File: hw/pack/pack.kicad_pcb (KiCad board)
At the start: 4 copper layers, 73.4 x 35 mm, 75 parts, among them J1 3.5mm locking, J2 USB-C, J3 SWD, Q1 DMG2305UX, SW1 recessed slide, U1 BT40NE, U2 PCM1840, U3 OPA1656, U4 TPS61023, U5 TLV75533P, U6 TLV75533P, U7 USBLC6-2SC6

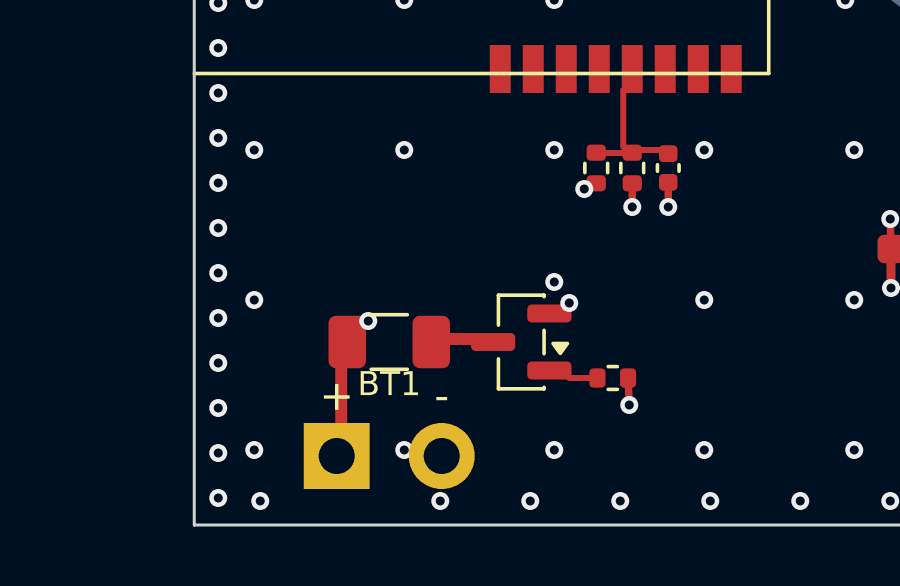
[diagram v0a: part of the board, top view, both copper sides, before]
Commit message: hw/pack: enclosure fit (fit.py + CadQuery test), mech outline from the layout, layout tests (#34)
mech/pack.py takes the real outline (73.4 x 35 mm, post notch), z0 +1.4 mm so
the module antenna clears the clip bosses, and the antenna overhang as a part.
fit.py checks board/parts/openings/lid features without CadQuery and renders
fit_top/fit_side.png; tests/mech/test_pack_fit.py does it with the STEP.
tests/test_pack_layout.py: DRC 0 errors, fab outputs fresh, netlist parity.

Co-Authored-By: Claude Opus 5.5 <noreply@anthropic.com>
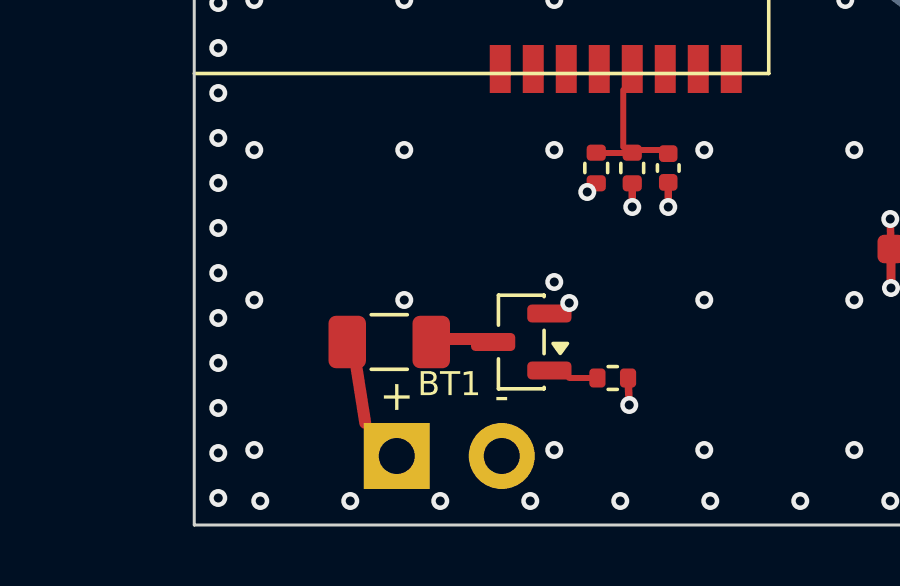
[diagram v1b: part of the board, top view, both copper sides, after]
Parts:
- moved BT1 2.00 mm to (80.5, 104.2)
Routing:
- net BAT+: track 10.5 -> 11.4 mm, vias 2 -> 1
- net GND: vias 205 -> 206

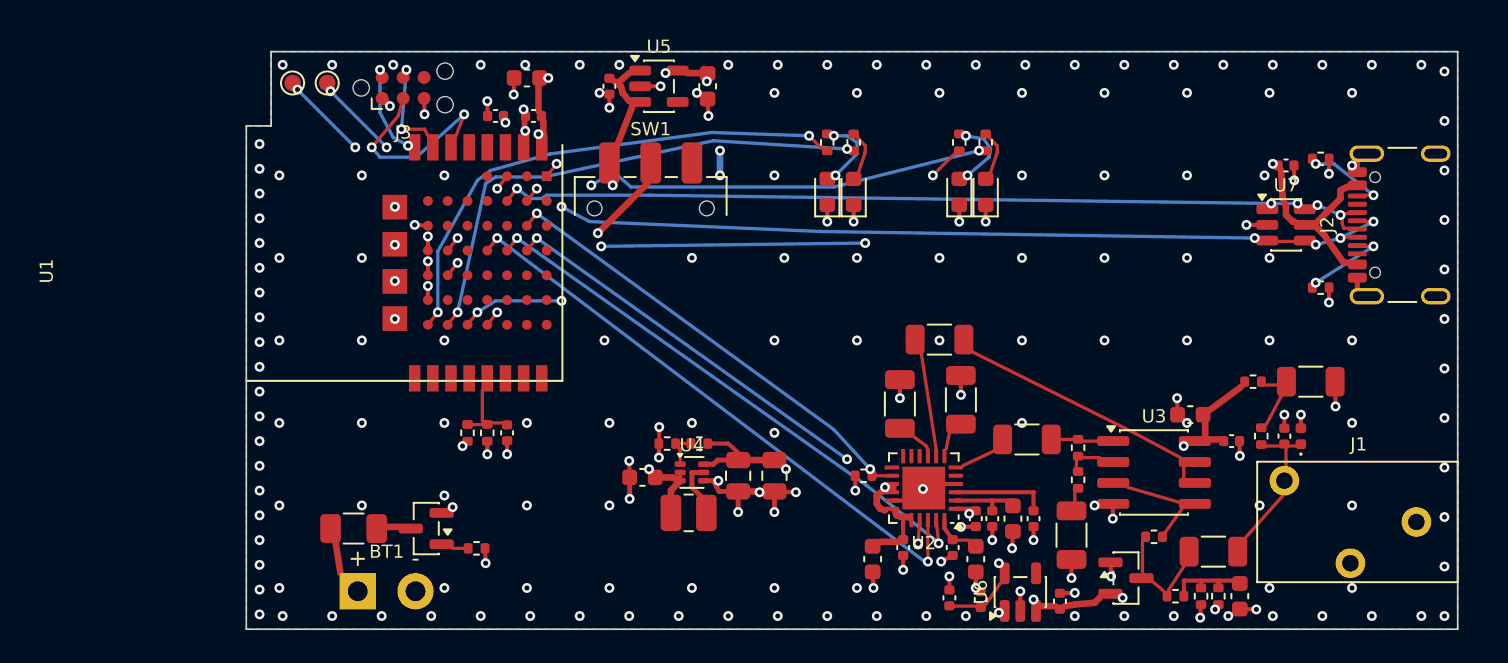
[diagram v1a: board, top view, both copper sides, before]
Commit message: hw/pack, mech: SJ1-3543 from datasheet, M2 board retention, light pipes, switch fork, CI pcb job (#34)
- SJ1-3543 footprint from Same Sky SJ1-354X (09/2024): 12x11.6x9.6 body, M6
  bushing through the wall from the inner face, axis 5.2 mm, anchors on GND
- H1/H2 M2 holes + printed pilot bosses (mech PCB_SCREWS), two rests
- lid light-pipe chimneys (lid prints outer-face-down), printed switch fork
  straddling SW1's right-angle actuator through a relocated slot
- mech comps() now the per-part envelope from the layout
- fit.py checks fork, chimneys, screws; CadQuery fit test mandatory under CI
- ci.yml: pcb job (KiCad 10 PPA) runs tests/test_pack_layout.py
- REVIEW: holder BH-18650-W and pigtail Molex 0731160017 chosen; with them
  PK-12 would be ~$38.2 > $35, prices.py left unchanged pending decision

Co-Authored-By: Claude Opus 5.5 <noreply@anthropic.com>
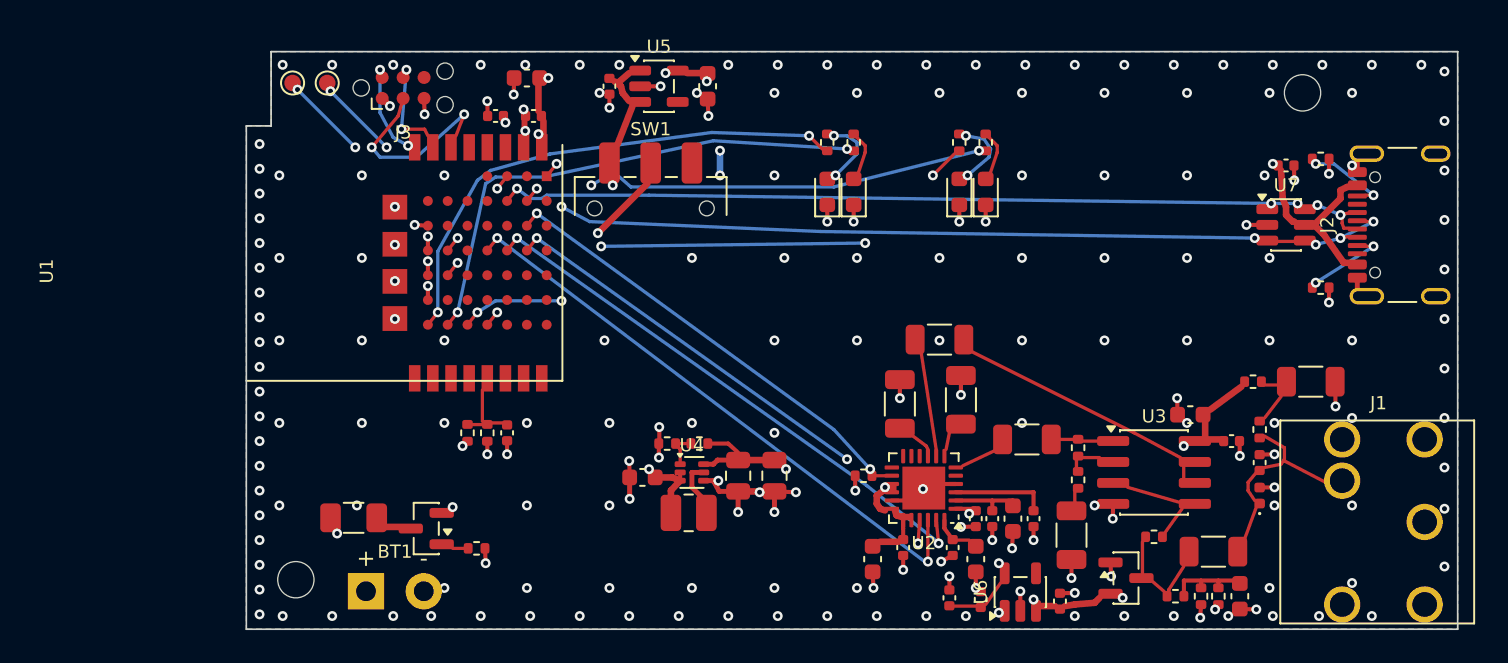
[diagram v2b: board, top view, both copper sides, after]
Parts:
- added H1: MountingHole_2.2mm_M2, MountingHole:MountingHole_2.2mm_M2, F.Cu at (75.0, 103.5)
- added H2: MountingHole_2.2mm_M2, MountingHole:MountingHole_2.2mm_M2, F.Cu at (136.0, 74.0)
- moved D5 4.38 mm to (133.4, 98.4)
- moved C9 2.19 mm to (133.4, 96.4)
- moved J1 1.00 mm to (146.4, 100.0)
- moved F1 0.65 mm to (78.5, 99.8)
- moved BT1 0.50 mm to (81.0, 104.2)
- moved R5 0.41 mm to (133.4, 94.4)
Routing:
- net MIC: track 6.01 -> 10.3 mm
- net BAT+: track 11.4 -> 11.8 mm, vias 1 -> 2
- net GND: track 67.4 -> 67.6 mm, vias 206 -> 203

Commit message: pack: cost-down to PK-12 $33.34: printed cell cradle + MYOUNG contacts, LCSC IPEX pigtail, priced M2 screws (#34)
- BT1: MYOUNG MY-18650-04-J/-05-J (LCSC C19184125/C19184124) in a printed
  cradle in the base (76 mm plate faces: spring 4.2-9.2 mm for 70-65 mm cells);
  the SMT BH-18650-B1BA002 holder is gone; footprint Cell_Wire_Pads
- pigtail: BAT Wireless BWIPX1-SMA-1.13L150 (LCSC C784404, $0.6015 @100), SMA
  cut off, ~100 mm + 31 mm wire whip; audit.py PIGTAIL_IL 0.46 <= 0.6 dB
- audit.py cutoff path includes the spring (0.10 ohm), cutoff stays 3.2 V
- 2 x M2x6 PT screws $0.112 (Fastener Superstore 585907)
- prices.py, bom.csv, pack_uk.csv (UK $34.81) updated

Co-Authored-By: Claude Opus 5.5 <noreply@anthropic.com>
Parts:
- BT1: value 18650 holder -> 18650 cradle contacts; footprint openpack:BH-18650-B1BA002 -> openpack:Cell_Wire_Pads

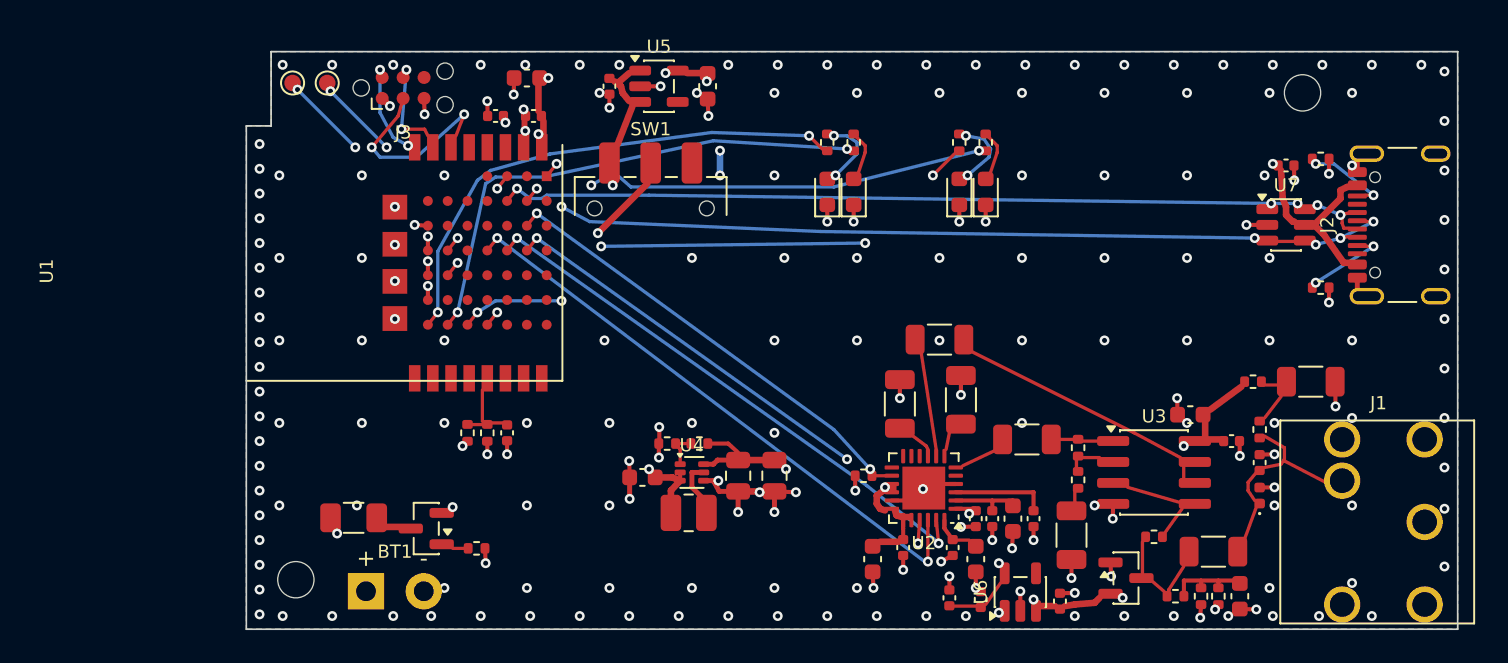
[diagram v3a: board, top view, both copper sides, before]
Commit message: pack: #104 review fixes: 1 mm L1 battery path, test points, clip inserts off the antenna, pigtail route, JLC LCSC/rotations (#34)
- router: 'bat' class (1.0 mm, L1 only, necks <=1.36 mm at small pads);
  SW1 on-throw moved to pin 3 so feed and VSYS don't cross; 40 mOhm path
- audit.py: cell path from the board tracks (121 mOhm total, est. spring):
  cutoff computes 3.2012 V -> rounds to 3.3 V (reported, not tuned)
- TP3-TP11 folded in from review-104-tps (415194b), TP5/TP9-11 moved
- mech: clip inserts to (-24,3)/(-24,17) under the board; PIGTAIL route,
  bend radius, tie-down; fit.py checks both
- outputs: LCSC # per BOM line (verified), DNP/CONSIGN, CPL rotation table
- tests: battery path layer/width/R, BOM LCSC-or-DNP, rotation table

Co-Authored-By: Claude Opus 5.5 <noreply@anthropic.com>
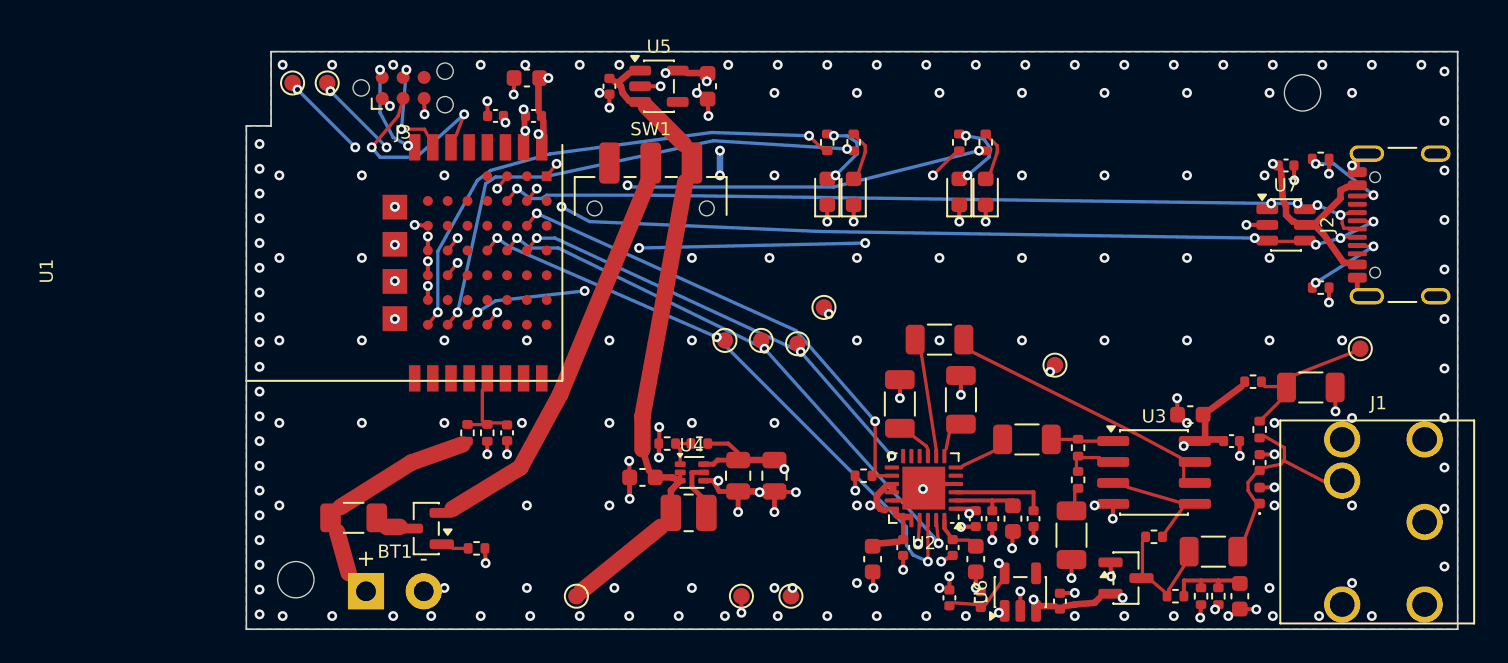
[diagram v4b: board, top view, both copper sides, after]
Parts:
- added TP10: I2S_FSYNC, TestPoint:TestPoint_Pad_D1.0mm, F.Cu at (103.2, 89.0)
- added TP11: I2S_SDOUT, TestPoint:TestPoint_Pad_D1.0mm, F.Cu at (105.4, 89.2)
- added TP3: VSYS, TestPoint:TestPoint_Pad_D1.0mm, F.Cu at (92.0, 104.5)
- added TP4: +5V, TestPoint:TestPoint_Pad_D1.0mm, F.Cu at (105.0, 104.5)
- added TP5: +3V3, TestPoint:TestPoint_Pad_D1.0mm, F.Cu at (107.0, 87.0)
- added TP6: +3V3A, TestPoint:TestPoint_Pad_D1.0mm, F.Cu at (121.0, 90.5)
- added TP7: +5V_BIAS, TestPoint:TestPoint_Pad_D1.0mm, F.Cu at (139.5, 89.5)
- added TP8: GND, TestPoint:TestPoint_Pad_D1.0mm, F.Cu at (102.0, 104.5)
- added TP9: I2S_BCLK, TestPoint:TestPoint_Pad_D1.0mm, F.Cu at (101.0, 89.0)
- moved C8 0.35 mm to (136.5, 91.8)
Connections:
- SW1 pad 1: VSYS -> (no net)
- SW1 pad 3: (no net) -> VSYS
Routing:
- net +3V3A: track 7.97 -> 18.0 mm, vias 2 -> 3
- net VSYS: track 26.8 -> 33.9 mm, vias 2 -> 0
- net +5V: track 47.2 -> 51.4 mm, vias 6 -> 7
- net +5V_BIAS: track 2.44 -> 6.08 mm
- net ADC_SHDNZ: track 27.2 -> 29.1 mm
- net I2S_SDOUT: track 32.1 -> 33.9 mm, vias 3 -> 4
- net +3V3: track 58.3 -> 60.0 mm, vias 10 -> 11
- net LED_CLIP: track 34.9 -> 33.8 mm
- net I2S_BCLK: track 36.2 -> 37.3 mm, vias 2 -> 3
- net I2S_FSYNC: track 34.0 -> 35.0 mm, vias 2 -> 3
- net GND: track 67.6 -> 68.5 mm, vias 203 -> 205
- net BAT+: track 11.8 -> 11.0 mm, vias 2 -> 0
- net LED_PEAK: track 34.0 -> 33.2 mm
- net VBAT_RP: track 23.3 -> 23.7 mm, vias 2 -> 0
